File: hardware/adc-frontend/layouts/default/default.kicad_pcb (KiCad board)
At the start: 4 copper layers, 142.2 x 111.6 mm, 144 parts

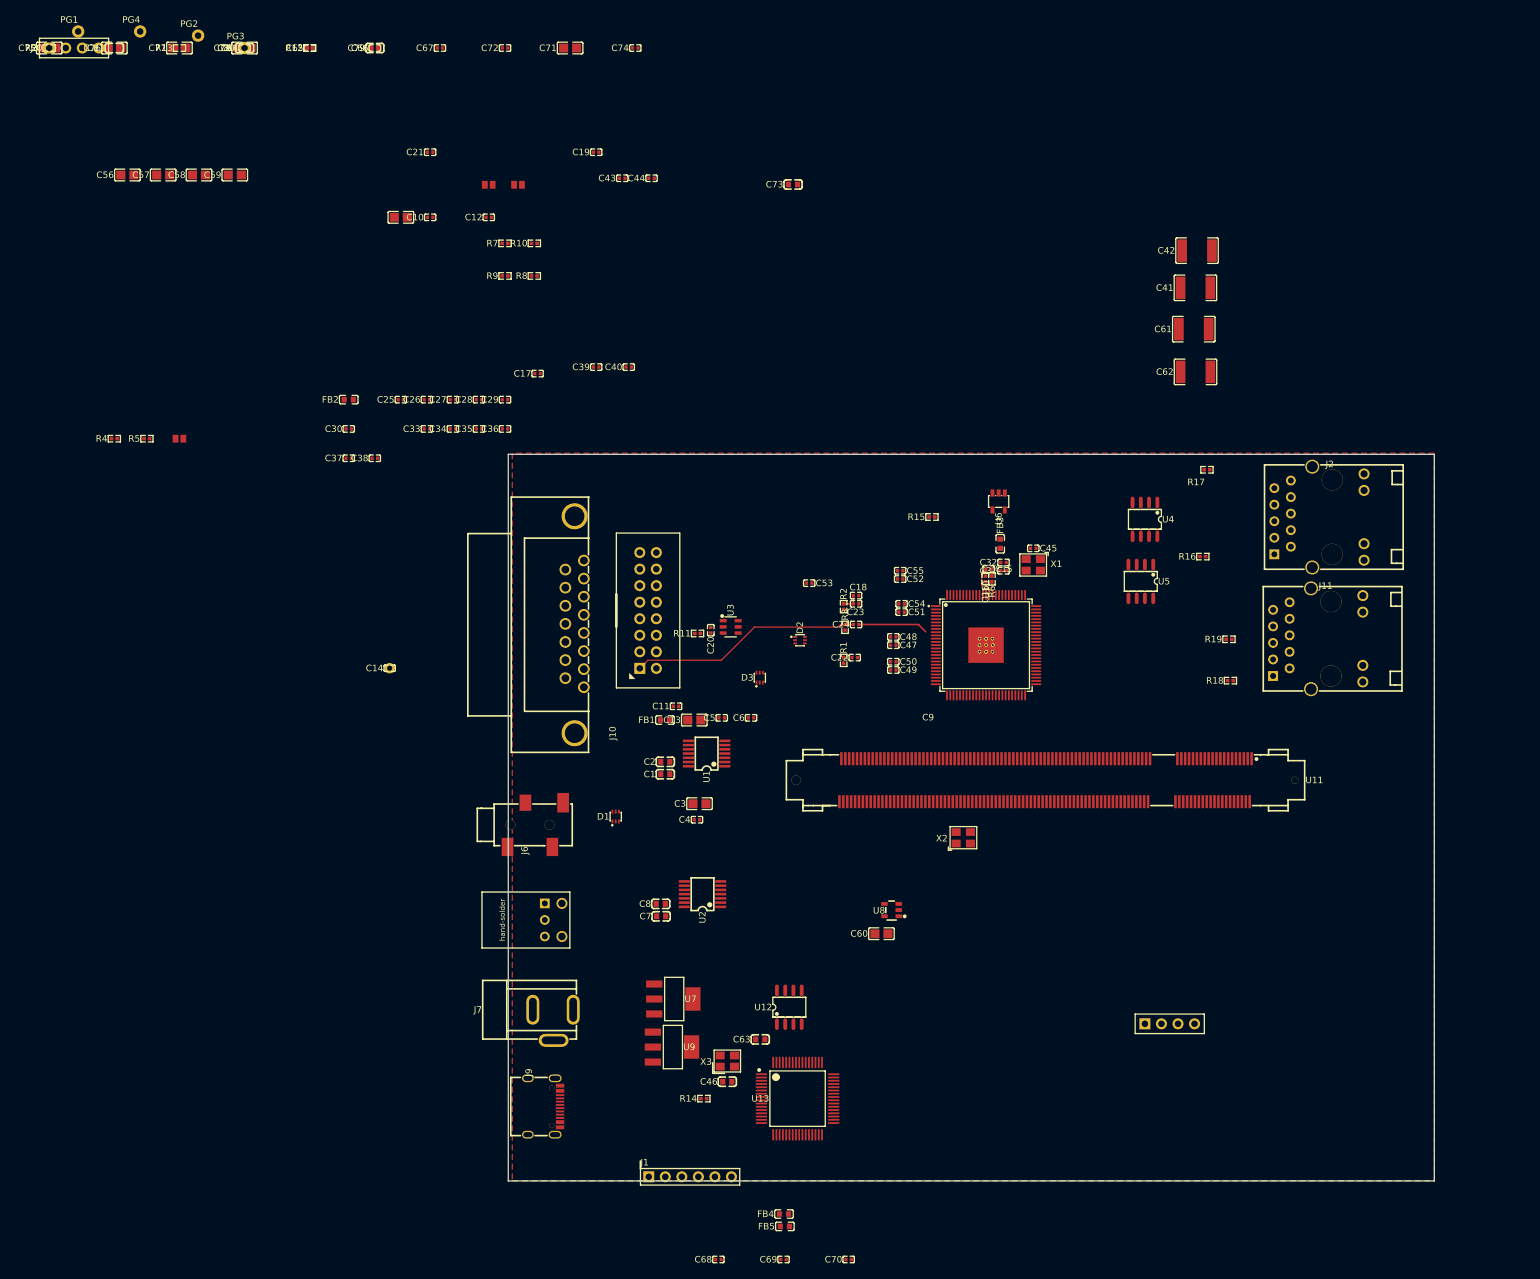
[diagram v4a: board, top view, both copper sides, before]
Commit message: 行欠け/横ずれを修正: 範囲を row/ts と同じ瞬間にFIFO先頭から取る
実機で 525行すべて一致(span_check 100%、対照実験も100%)。Viewerの画面でも
行欠けが消えたことを確認した。

原因は送信側でヘッダの値の取り方が揃っていなかったこと。

    row / ts / frame  送出開始時にFIFO先頭から直接スナップショット
    offset_px         先頭を毎サイクル追いかける2段レジスタ経由  ← これ

両者が同じFIFOエントリを指す保証がなく、範囲だけが fifo_depth ライン遅れて乗って
いた(depth 4→4ライン、8→8ライン の2点で確認)。内容のある行が空(count_px=0)で
送られるので行が欠け、範囲が隣の行のものになると絵が横にずれた。当初「全幅の明るい
横線の直後3行が2サンプル早い」と見えていたのも同じ原因である。

修正は、範囲も row/ts と同じ瞬間に先頭からラッチし、派生値(断片数・長さ)は次の
サイクル(FSMに LPREP 状態を追加)でそのラッチ値だけから作る。同一エントリ由来が
構造的に保証される。組合せ経路を短く保つための段分けは維持した(組合せで作ると
sys が 42.4MHz まで落ちた実績があるため)。1ライン当たり1サイクル増えるだけ。

不要になった span_rdy(範囲が追いつくまで待つ仕掛け)は撤去した。待っても別エントリ
を指す可能性が残る対処だった。

場所の特定に使った3段の窓を残す:
  key 0x31/0x32  指定行の範囲を pix ドメインで直読(push時点の生値)
  key 0x33       cap_drops
  key 0x34       pop時のFIFO先頭の {row, x_lo, x_hi}
これで「pixもFIFO出口も正しいのに電線だけ違う」ことを示せた。

否定された筋(実測):
- DATACLKの位相/PLL/電源。ts から offset_px を引いた隣接差が全524箇所で htotal と
  一致し、HSOUTとDATACLKの関係は1行も動いていない。基板の設計変更は不要
- メタFIFOの溢れ。動作中の cap_drops は0(購読していない間だけ溢れる)
- 面の追い越し。nface=16 でも変化なし
- キャプチャの非黒判定。pixドメインの窓で内容と一致

nface=16 / fifo_depth=8 は切り分けのための暫定値でまだ戻していない(TODO 1)。
seed 既定は 5(この構成で eth_rx が seed 3 では 116.65MHz、seed 5 で 136.09MHz)。

Co-Authored-By: Claude Opus 5 (1M context) <noreply@anthropic.com>
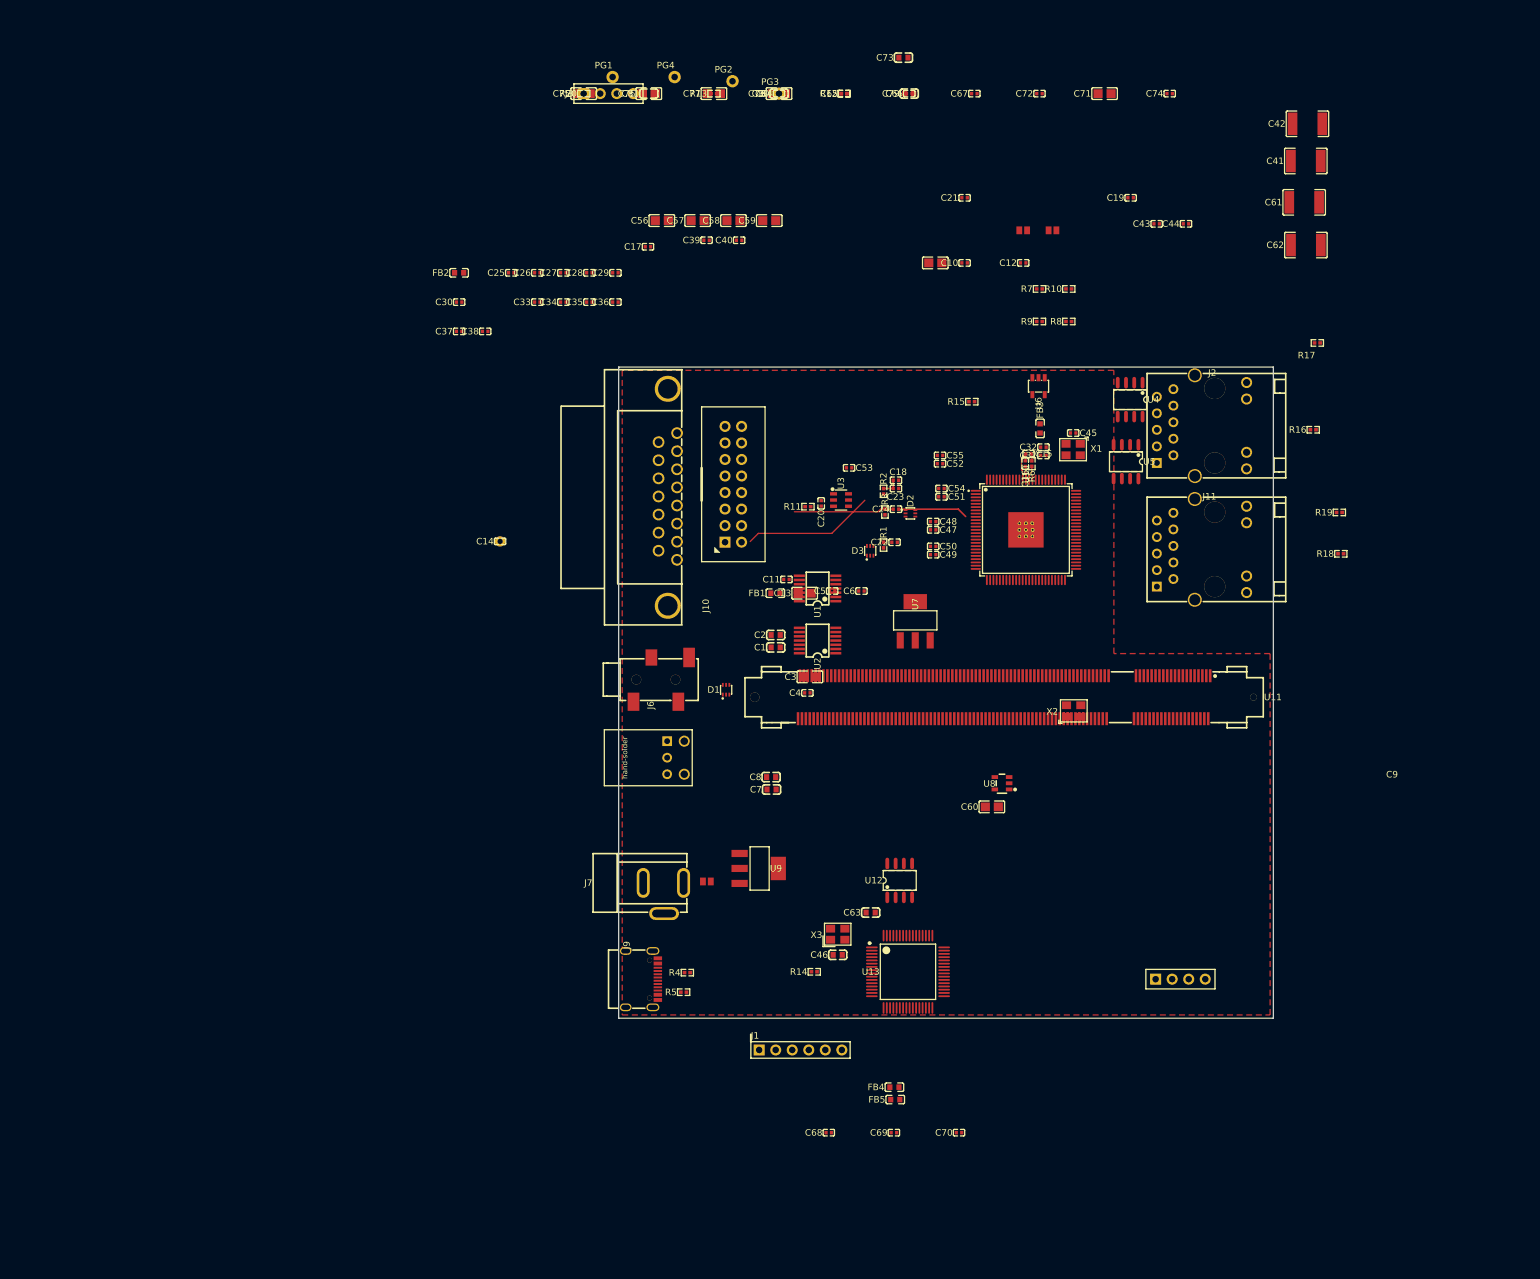
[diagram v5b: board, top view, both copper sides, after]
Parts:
- moved R4 120.3 mm to (98.0, 142.0)
- moved R5 118.4 mm to (97.4, 145.0)
- moved JP3 105.8 mm to (101.0, 128.0)
- moved C10 82.4 mm to (140.6, 33.0)
- moved C12 82.4 mm to (149.6, 33.0)
- moved C19 82.4 mm to (166.1, 23.0)
- moved C21 82.4 mm to (140.6, 23.0)
- moved C43 82.4 mm to (170.1, 27.0)
- moved C44 82.4 mm to (174.6, 27.0)
- moved C66 82.4 mm to (132.1, 7.00)
- moved C67 82.4 mm to (142.1, 7.00)
- moved C71 82.4 mm to (162.1, 7.00)
- moved C72 82.4 mm to (152.1, 7.00)
- moved C74 82.4 mm to (172.1, 7.00)
- moved C79 82.4 mm to (132.1, 7.00)
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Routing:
- net 129: track 10.8 -> 0.00 mm
- net c_ac-power-lv-1: track 0.00 -> 10.8 mm
- added copper zone on In2.Cu, net p3v3_a
- added copper zone on In2.Cu, net p3v3_io
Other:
- board size 142.2 x 111.6 mm -> 100.5 x 100 mm

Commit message: CZ-612D の正面図イラストを追加(枠として使う)
client/assets/cz612d.svg。写真ではなく作図。寸法は実機写真から採寸した値を
そのまま座標に使い、<desc> に一覧を残してある。

  キャビネット  0..1013 x 0..956    (比 1.059)
  ガラス開口部  105..902 x 127..724 (797x598 = 4:3)
  ベゼル        54..952 x 95..788   (余白 上32/左右50/下64)
  ふた          150..778 x 824..956 (下端=筐体下端)
  スタンド      首 956..990 / 台座 990..1057

開口部は even-odd で「穴」にしてあるので、後ろに映像を置けばそのまま枠になる。

実機写真は斜め上から撮っているので、正面図では見えない面は描かない(台座の天面
45pxぶんを落とし、高さは前面の垂直面だけにした)。

ふたの合わせ目は正面写真と近接写真の2つの独立した測定で一致した(左端 150 /
右端 778)。ディテールの要なので溝の線で描く。ふたの面は塗らない。塗ると body
グラデーションが矩形内で描き直されてまわりと繋がらず、浮き上がって見える。
同じ理由で前面パネルの中間板も置かない。段差は面の色ではなく溝で見せる。

開口部の比は実測 1.316 だったが 4:3(1.3328)に合わせた。管面モデルの4:3の映像を
そのまま入れると1.3%横に伸びるため。高さ598を保ち幅を+10、中心は不変。

作図中に3つの誤りを出した。いずれも背景が白いブラウザで見て初めて露見し、
自分の合成プレビュー(穴を暗いグレーで埋めていた)が問題を隠していた:
- inner の even-odd の外周が開口部より小さく、開口部に半透明の帯がはみ出した
- ガラスの映り込みが映像の上に薄いグレーの模様として乗った(撤去)
- 中間板とふたの面塗りでグラデーションが分断された(撤去)

対策として、白背景と暗背景の両方でプレビューを作り、even-odd を使うパスは
「外周が開口部を完全に含むか」を数値で検算するようにした。確認の手段が問題を
隠してはいけないという点で、design-notes.md の「測定系を先に疑う」と同じ話。

Co-Authored-By: Claude Opus 5 (1M context) <noreply@anthropic.com>
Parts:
- moved C62 60.2 mm to (164.0, 83.0), turned to 180 degrees
- moved U4 58.5 mm to (155.9, 111.6), turned to -90 degrees
- moved C61 55.3 mm to (164.0, 71.0), turned to 180 degrees
- moved C41 54.9 mm to (164.0, 64.0), turned to 180 degrees
- moved C42 49.8 mm to (164.0, 52.0), turned to 180 degrees
- moved U5 48.7 mm to (165.4, 112.2), turned to -90 degrees
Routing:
- added copper zone on B.Cu, net chassis
- added copper zone on F.Cu, net chassis
- added copper zone on In1.Cu, net chassis
- added copper zone on In2.Cu, net chassis

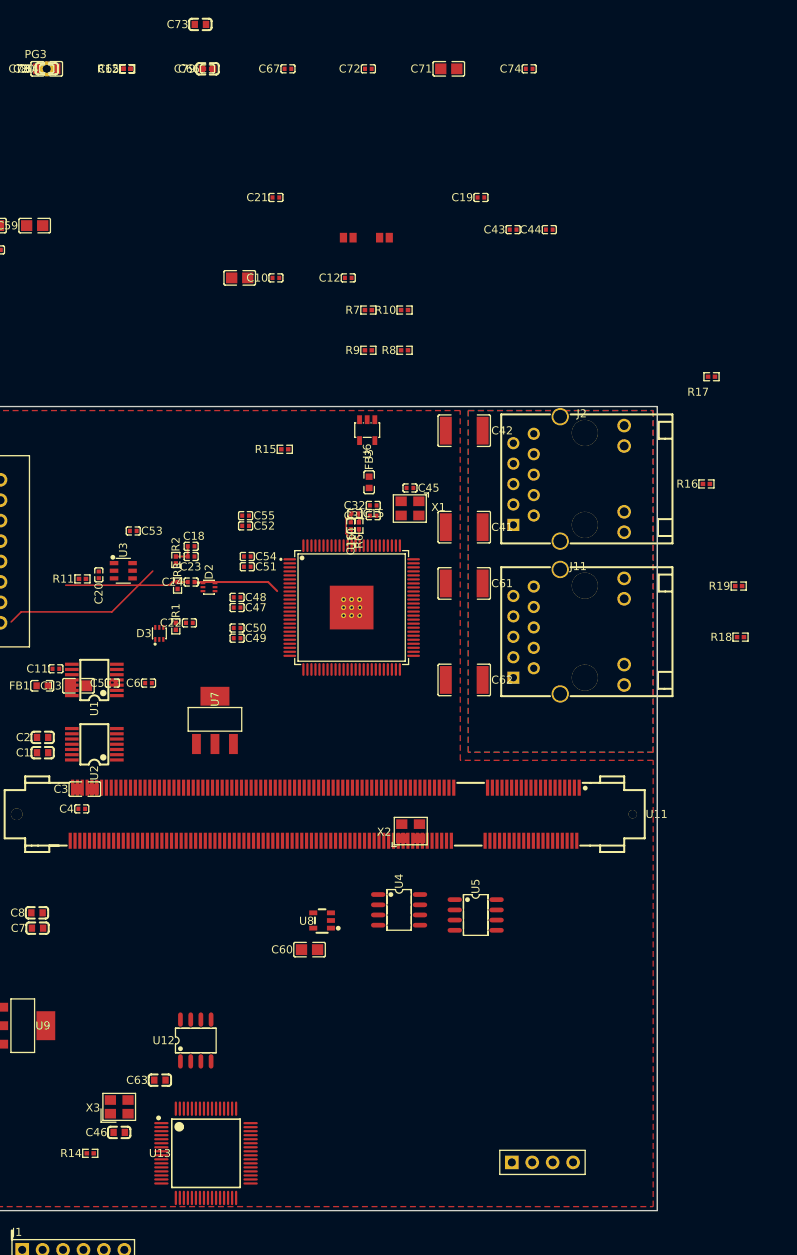
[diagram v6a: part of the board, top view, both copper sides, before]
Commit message: 枠(CZ-612D)をViewerへ組み込み、宛先指定なしで使えるようにする
## 枠

client/src/bezel.rs を追加。SVGを include_str! で埋め込み、resvg で起動時に
1回ラスタライズしてテクスチャに保持する。必要な幅が変わったときだけ作り直し、
幅は64px刻みに丸めてリサイズ中に作り直し続けないようにした。Retinaの実画素数で
焼くのでぼけない。

枠ありのときは考え方が変わる:
  領域に収めるもの  枠なし=管面        枠あり=枠全体
  管面の縦横比      tube_aspect        開口部の比(枠は実在モニタの寸法)
  描画順            管面のみ           管面 → 枠を重ねる(開口部が抜けている)

開口部の座標はSVGから読めないので Rust 側の定数として持つ。assets/cz612d.svg の
<desc> と一致させること。片方だけ直すと絵と映像がずれる。

テストを3つ入れた。作図中に開口部へ半透明の帯がはみ出す不具合を2回出しており、
どちらも暗い背景の合成では見えず白背景で露見したので、背景に依らず捕まえられる
形にしてある(screen_area_is_transparent)。

UI: 「枠」プルダウン(なし / SHARP CZ-612D)と「表示」チェックボックス。
選択を保ったまま出し入れできるので機種を選び直さずに見比べられる。B キーでも
切り替わる。Tab で操作パネルを出し入れ。どちらも設定に保存する。

映像が無くても枠は描くようにした。実機のCRTは映像が無くても筐体があるので、
待機中に枠だけ消えるのは不自然。開口部は黒にして待機表示を中に出す。

## 直した不具合

- パネル/枠のトグルでウィンドウが縮み続けた。トグル時に want_fit を立てていたが、
  切り替えた直後の last_avail/last_tex は「切り替わる前のレイアウト」の値なので
  毎回ずれ、繰り返すと累積した。トグルでは大きさを変えない
- フルスクリーンで画が左に寄った。フルスクリーン中に InnerSize を送ると要求が
  部分的にしか効かずレイアウトが中途半端に残る。フルスクリーンでは何もしない

## 宛先指定なしで使えるようにする

既定は元からブロードキャスト(255.255.255.255)だったが、運用で --board を
指定していたため ifconfig alias が必要になっていた。ユニキャスト指定で3秒間
応答が無ければブロードキャストへ落とすようにした(逆の昇格はしない。宛先
サブネットへの経路が必要になるため)。UIは指定値ではなく実際の宛先を出す。

実測: 192.168.11.21 だけに束縛してブロードキャストで購読すると、192.168.10.50 から
LINE 77502 / MODE 996 が届いた。--board なしのヘッドレスでも 247フレーム / ロス0。

サブネットが違っても届く理由は、LiteEth にサブネットマスクもゲートウェイも無く
(liteeth/core/arp.py)宛先IPをそのままARPで引くため。同じL2セグメントなら成立し、
間にルータがあると成立しない。

帯域: ブロードキャストは Viewer が送る 40B×0.5回/秒 だけ。映像は sub_ip への
ユニキャストなのでスイッチはMacのポートにしか流さない。

## docs/design-notes.md に「実機を動かすときの準備」を追加

- SRAMとフラッシュの違い。SRAMだけに書いて作業を続けると電源で古い版に戻る
  (実際これで修正済みの不具合が再発し、ネットワークだけの問題と誤診した)
- --board を付けなければエイリアスは不要。付けたときだけ経路が必要
- 未対応の懸念: 255.255.255.255 をどのインターフェースから出すかはOS任せなので、
  Wi-Fiと有線が両方有効だと届かない可能性がある。有線1本なら問題にならないので
  後回しにしている
- 購読先はボードに1つだけ。Viewerと測定ツールが取り合う

Co-Authored-By: Claude Opus 5 (1M context) <noreply@anthropic.com>
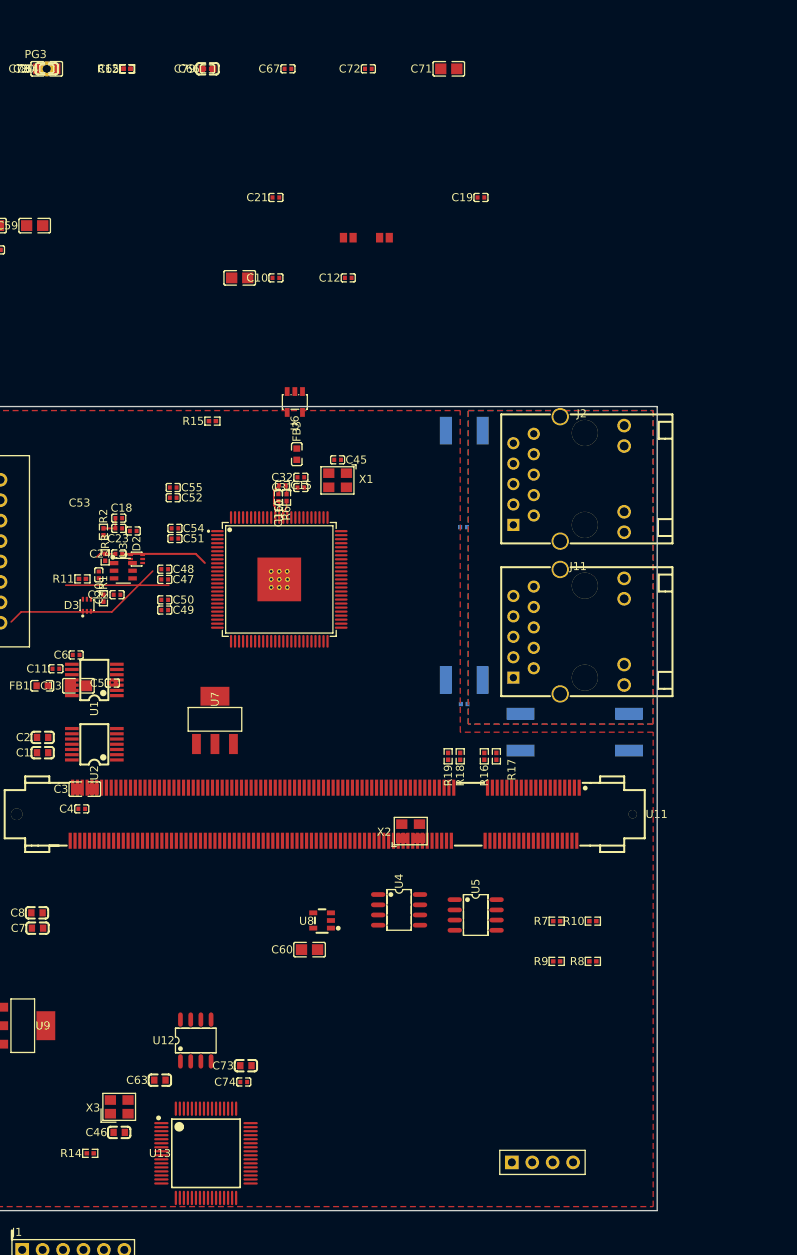
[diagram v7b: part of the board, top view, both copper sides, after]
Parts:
- C41, C42, C43, C44, C61, C62: moved to B.Cu
- moved C74 130.9 mm to (136.6, 133.0)
- moved C73 129.6 mm to (136.8, 131.0)
- moved R10 79.5 mm to (180.0, 113.0)
- moved R7 79.5 mm to (175.5, 113.0)
- moved R8 79.5 mm to (180.0, 118.0)
- moved R9 79.5 mm to (175.5, 118.0)
- moved C44 59.9 mm to (164.0, 86.0), turned to 180 degrees
- moved R17 54.3 mm to (168.0, 92.5), turned to 90 degrees
- moved R16 43.7 mm to (166.5, 92.5), turned to 90 degrees
- moved R19 41.9 mm to (162.0, 92.5), turned to 90 degrees
- moved R18 37.9 mm to (163.5, 92.5), turned to 90 degrees
- moved C43 37.5 mm to (163.9, 64.0), turned to 180 degrees
- moved C62 21.5 mm to (184.5, 89.5), turned to -90 degrees
- moved C61 19.8 mm to (171.0, 89.5), turned to -90 degrees
- moved C41 19.0 mm to (164.0, 83.0)
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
